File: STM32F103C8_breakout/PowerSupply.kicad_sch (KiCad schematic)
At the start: 6 parts, among them J20 USB-C, U2 BUCK_REG_3.3V

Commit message: Worked on PCB Layout
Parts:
- J20: footprint CONN_1054500101_MOL -> CONN_USBC:CONN_1054500101_MOL
- U2: footprint MLF-8_ML_MCH -> 3.3V_Buck:MLF-8_ML_MCH
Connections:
- net USB_OUT_MCU_IN renamed Vdd
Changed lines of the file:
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@@
 		)
 	)
-	(label "USB_OUT_MCU_IN"
+	(label "Vdd"
 		(at 227.33 72.39 0)
 		(effects
@@
 			)
 		)
-		(property "Footprint" "MLF-8_ML_MCH"
+		(property "Footprint" "3.3V_Buck:MLF-8_ML_MCH"
 			(at 135.89 59.69 0)
 			(hide yes)
@@
 			)
 		)
-		(property "Footprint" "CONN_1054500101_MOL"
+		(property "Footprint" "CONN_USBC:CONN_1054500101_MOL"
 			(at 55.88 57.15 0)
 			(hide yes)

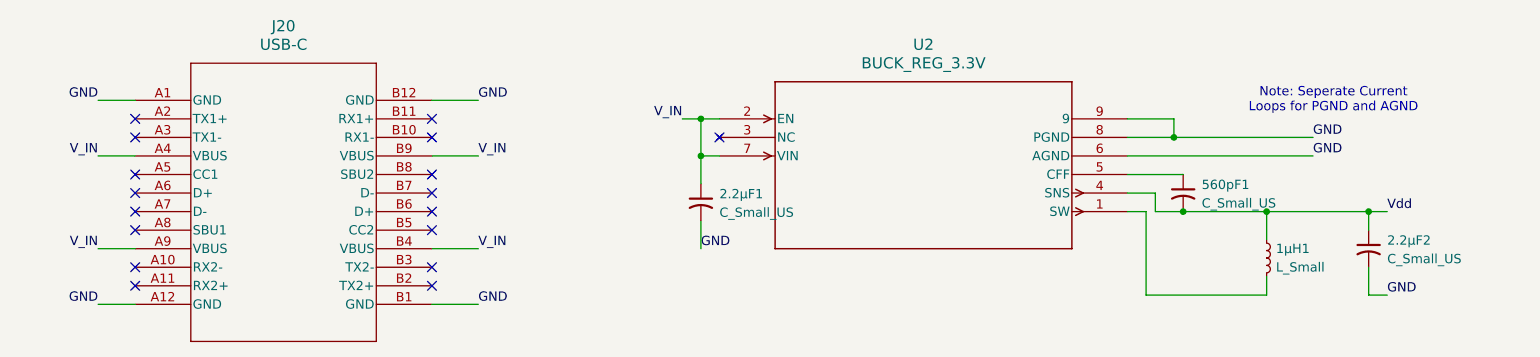
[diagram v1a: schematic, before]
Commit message: Completed PCB Layoutx
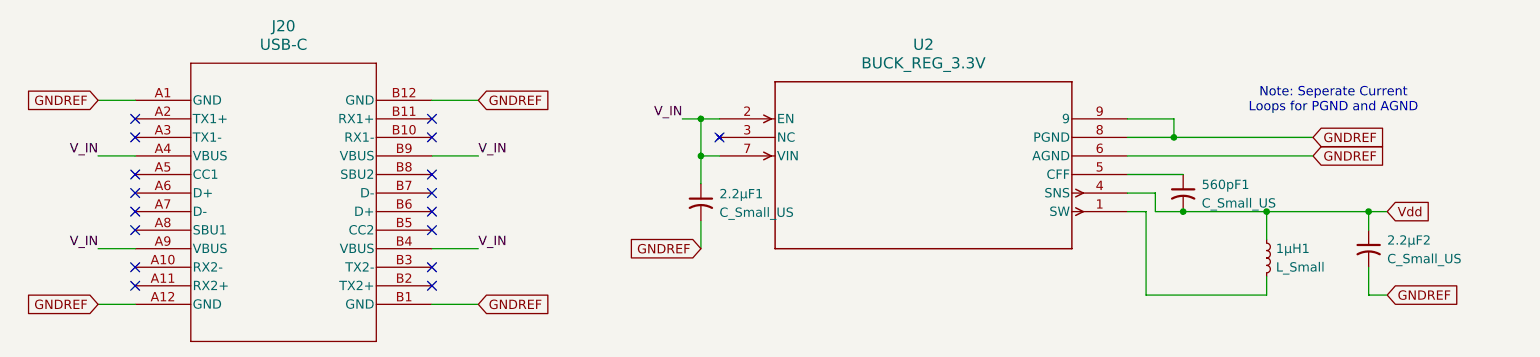
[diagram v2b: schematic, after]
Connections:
- net GND renamed GNDREF
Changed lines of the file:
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@@
 		)
 	)
-	(label "GND"
+	(label "V_IN"
+		(at 50.8 64.77 180)
+		(effects
+			(font
+				(size 1.27 1.27)
+			)
+			(justify right bottom)
+		)
+	)
+	(label "V_IN"
+		(at 50.8 77.47 180)
+		(effects
+			(font
+				(size 1.27 1.27)
+			)
+			(justify right bottom)
+		)
+	)
+	(label "V_IN"
+		(at 102.87 64.77 0)
+		(effects
+			(font
+				(size 1.27 1.27)
+			)
+			(justify left bottom)
+		)
+	)
+	(label "V_IN"
+		(at 102.87 77.47 0)
+		(effects
+			(font
+				(size 1.27 1.27)
+			)
+			(justify left bottom)
+		)
+	)
+	(global_label "GNDREF"
+		(shape input)
+		(at 102.87 85.09 0)
+		(fields_autoplaced yes)
+		(effects
+			(font
+				(size 1.27 1.27)
+			)
+			(justify left)
+		)
+		(property "Intersheetrefs" "${INTERSHEET_REFS}"
+			(at 113.2333 85.09 0)
+			(hide yes)
+			(show_name no)
+			(do_not_autoplace no)
+			(effects
+				(font
+					(size 1.27 1.27)
+				)
+				(justify left)
+			)
+		)
+	)
+	(global_label "GNDREF"
+		(shape input)
+		(at 102.87 57.15 0)
+		(fields_autoplaced yes)
+		(effects
+			(font
+				(size 1.27 1.27)
+			)
+			(justify left)
+		)
+		(property "Intersheetrefs" "${INTERSHEET_REFS}"
+			(at 113.2333 57.15 0)
+			(hide yes)
+			(show_name no)
+			(do_not_autoplace no)
+			(effects
+				(font
+					(size 1.27 1.27)
+				)
+				(justify left)
+			)
+		)
+	)
+	(global_label "GNDREF"
+		(shape input)
+		(at 133.35 77.47 180)
+		(fields_autoplaced yes)
+		(effects
+			(font
+				(size 1.27 1.27)
+			)
+			(justify right)
+		)
+		(property "Intersheetrefs" "${INTERSHEET_REFS}"
+			(at 122.9867 77.47 0)
+			(hide yes)
+			(show_name no)
+			(do_not_autoplace no)
+			(effects
+				(font
+					(size 1.27 1.27)
+				)
+				(justify right)
+			)
+		)
+	)
+	(global_label "Vdd"
+		(shape input)
+		(at 227.33 72.39 0)
+		(fields_autoplaced yes)
+		(effects
+			(font
+				(size 1.27 1.27)
+			)
+			(justify left)
+		)
+		(property "Intersheetrefs" "${INTERSHEET_REFS}"
+			(at 233.7018 72.39 0)
+			(hide yes)
+			(show_name no)
+			(do_not_autoplace no)
+			(effects
+				(font
+					(size 1.27 1.27)
+				)
+				(justify left)
+			)
+		)
+	)
+	(global_label "GNDREF"
+		(shape input)
+		(at 217.17 64.77 0)
+		(fields_autoplaced yes)
+		(effects
+			(font
+				(size 1.27 1.27)
+			)
+			(justify left)
+		)
+		(property "Intersheetrefs" "${INTERSHEET_REFS}"
+			(at 227.5333 64.77 0)
+			(hide yes)
+			(show_name no)
+			(do_not_autoplace no)
+			(effects
+				(font
+					(size 1.27 1.27)
+				)
+				(justify left)
+			)
+		)
+	)
+	(global_label "GNDREF"
+		(shape input)
+		(at 227.33 83.82 0)
+		(fields_autoplaced yes)
+		(effects
+			(font
+				(size 1.27 1.27)
+			)
+			(justify left)
+		)
+		(property "Intersheetrefs" "${INTERSHEET_REFS}"
+			(at 237.6933 83.82 0)
+			(hide yes)
+			(show_name no)
+			(do_not_autoplace no)
+			(effects
+				(font
+					(size 1.27 1.27)
+				)
+				(justify left)
+			)
+		)
+	)
+	(global_label "GNDREF"
+		(shape input)
+		(at 217.17 62.23 0)
+		(fields_autoplaced yes)
+		(effects
+			(font
+				(size 1.27 1.27)
+			)
+			(justify left)
+		)
+		(property "Intersheetrefs" "${INTERSHEET_REFS}"
+			(at 227.5333 62.23 0)
+			(hide yes)
+			(show_name no)
+			(do_not_autoplace no)
+			(effects
+				(font
+					(size 1.27 1.27)
+				)
+				(justify left)
+			)
+		)
+	)
+	(global_label "GNDREF"
+		(shape input)
 		(at 50.8 85.09 180)
-		(effects
-			(font
-				(size 1.27 1.27)
-			)
-			(justify right bottom)
-		)
-	)
-	(label "Vdd"
-		(at 227.33 72.39 0)
-		(effects
-			(font
-				(size 1.27 1.27)
-			)
-			(justify left bottom)
-		)
-	)
-	(label "V_IN"
-		(at 50.8 64.77 180)
-		(effects
-			(font
-				(size 1.27 1.27)
-			)
-			(justify right bottom)
-		)
-	)
-	(label "GND"
-		(at 217.17 64.77 0)
-		(effects
-			(font
-				(size 1.27 1.27)
-			)
-			(justify left bottom)
-		)
-	)
-	(label "V_IN"
-		(at 50.8 77.47 180)
-		(effects
-			(font
-				(size 1.27 1.27)
-			)
-			(justify right bottom)
-		)
-	)
-	(label "GND"
-		(at 227.33 83.82 0)
-		(effects
-			(font
-				(size 1.27 1.27)
-			)
-			(justify left bottom)
-		)
-	)
-	(label "V_IN"
-		(at 102.87 64.77 0)
-		(effects
-			(font
-				(size 1.27 1.27)
-			)
-			(justify left bottom)
-		)
-	)
-	(label "GND"
+		(fields_autoplaced yes)
+		(effects
+			(font
+				(size 1.27 1.27)
+			)
+			(justify right)
+		)
+		(property "Intersheetrefs" "${INTERSHEET_REFS}"
+			(at 40.4367 85.09 0)
+			(hide yes)
+			(show_name no)
+			(do_not_autoplace no)
+			(effects
+				(font
+					(size 1.27 1.27)
+				)
+				(justify right)
+			)
+		)
+	)
+	(global_label "GNDREF"
+		(shape input)
 		(at 50.8 57.15 180)
-		(effects
-			(font
-				(size 1.27 1.27)
-			)
-			(justify right bottom)
-		)
-	)
-	(label "GND"
-		(at 102.87 85.09 0)
-		(effects
-			(font
-				(size 1.27 1.27)
-			)
-			(justify left bottom)
-		)
-	)
-	(label "V_IN"
-		(at 102.87 77.47 0)
-		(effects
-			(font
-				(size 1.27 1.27)
-			)
-			(justify left bottom)
-		)
-	)
-	(label "GND"
-		(at 217.17 62.23 0)
-		(effects
-			(font
-				(size 1.27 1.27)
-			)
-			(justify left bottom)
-		)
-	)
-	(label "GND"
-		(at 102.87 57.15 0)
-		(effects
-			(font
-				(size 1.27 1.27)
-			)
-			(justify left bottom)
-		)
-	)
-	(label "GND"
-		(at 133.35 77.47 0)
-		(effects
-			(font
-				(size 1.27 1.27)
-			)
-			(justify left bottom)
-		)
-	)
+		(fields_autoplaced yes)
+		(effects
+			(font
+				(size 1.27 1.27)
+			)
+			(justify right)
+		)
+		(property "Intersheetrefs" "${INTERSHEET_REFS}"
+			(at 40.4367 57.15 0)
+			(hide yes)
+			(show_name no)
+			(do_not_autoplace no)
+			(effects
+				(font
+					(size 1.27 1.27)
+				)
+				(justify right)
+			)
+		)
+	)
